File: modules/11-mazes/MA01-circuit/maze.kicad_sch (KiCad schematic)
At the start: 7 parts, among them J1 MODULE Connector

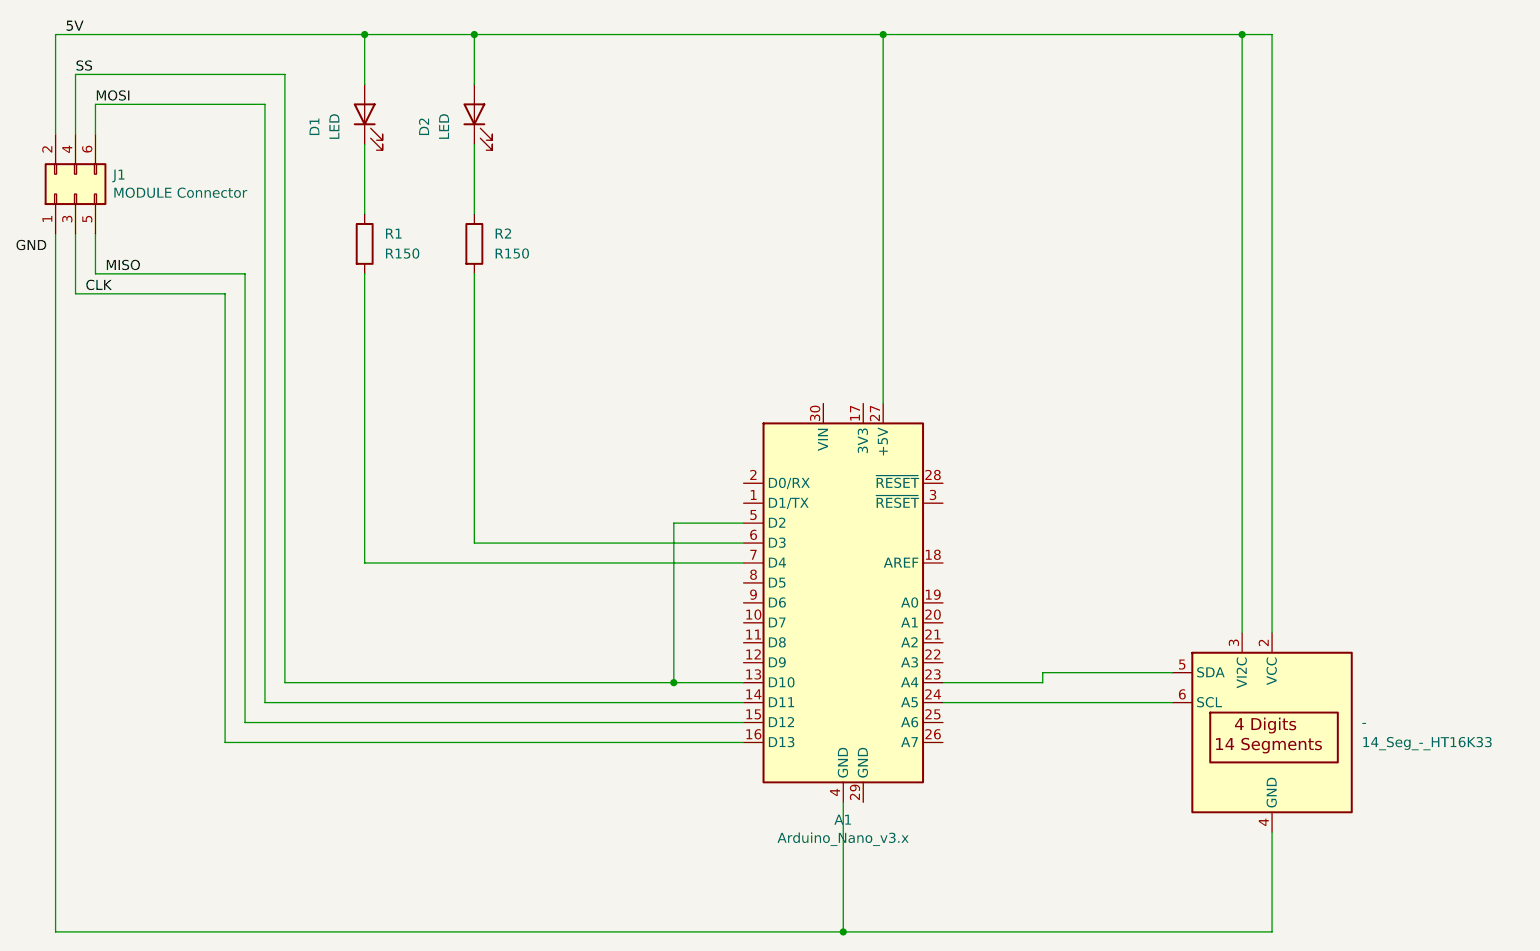
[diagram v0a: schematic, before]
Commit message: cleanup circuit
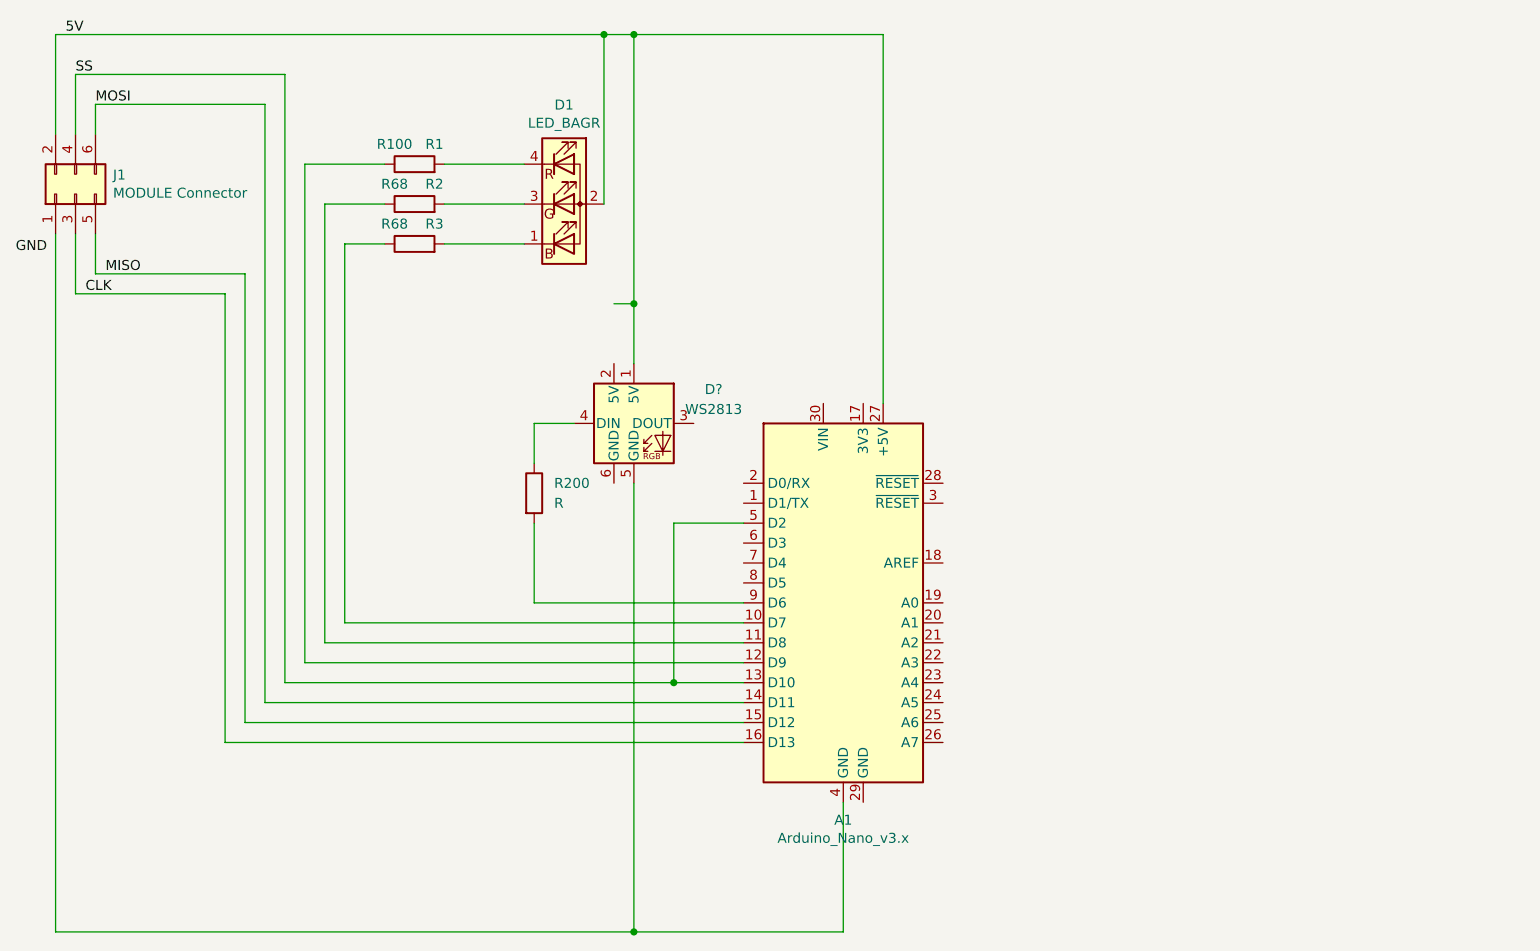
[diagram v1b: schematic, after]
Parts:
- removed -: 14_Seg_-_HT16K33, symbol New_Library:14_Seg_-_HT16K33
- removed D1, D2: LED, symbol Device:LED
- added D1: LED_BAGR, symbol Device:LED_BAGR
- added D?: WS2813, LED_SMD:LED_WS2812_PLCC6_5.0x5.0mm_P1.6mm, symbol LED:WS2813
- added R200: R, symbol Device:R
- added R3: R68, symbol Device:R
- R1: value R150 -> R100
- R2: value R150 -> R68
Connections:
- net 5V: now also D1.2 (A), D?.1 (5V)
- net at A1.4 (GND), J1.1 (Pin_1): now also D?.5 (GND)
- net at A1.10 (D7): now also R3.1
- net at A1.11 (D8): now also R2.1
- net at A1.12 (D9): now also R1.1
- net at A1.6 (D3): no longer R2.2
- net at A1.7 (D4): no longer R1.2
- net at A1.9 (D6): now also R200.2
- new net: D1.1 (BK), R3.2
- new net: D1.3 (GK), R2.2
- new net: D1.4 (RK), R1.2
- new net: D?.4 (DIN), R200.1
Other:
- title: Schaltplan Modul Clock (01) -> Schaltplan Modul Mazes (11)
